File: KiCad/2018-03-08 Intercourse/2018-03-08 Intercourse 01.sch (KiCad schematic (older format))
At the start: 15 parts

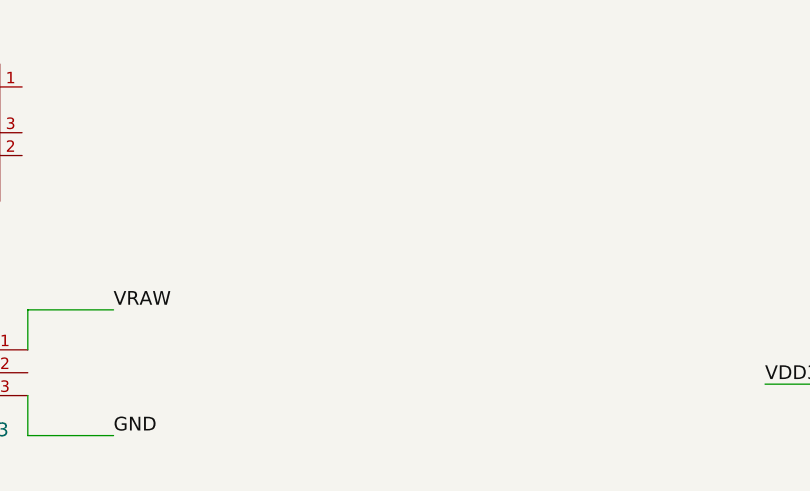
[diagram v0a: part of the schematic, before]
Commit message: added supercap charger
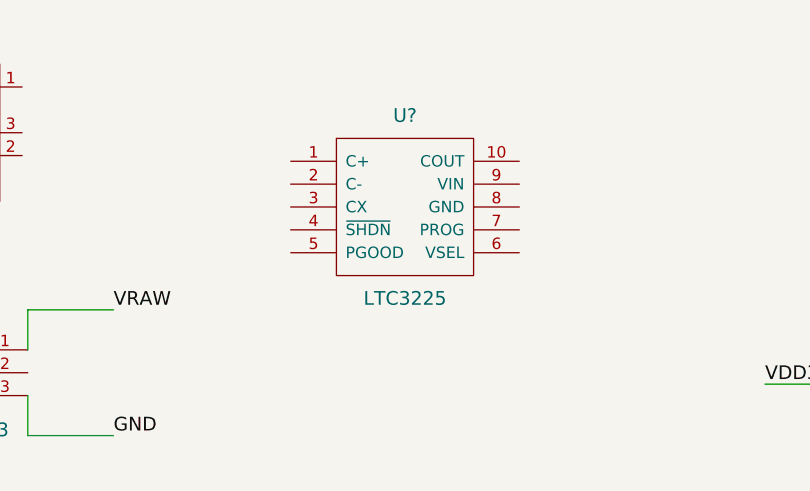
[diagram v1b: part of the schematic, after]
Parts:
- added U?: LTC3225, symbol LTC3225
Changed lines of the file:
@@
 LIBS:w25q-flash
 LIBS:murata-dmf3-supercap
+LIBS:LTC3225
 LIBS:2018-03-08 Intercourse 01-cache
 EELAYER 25 0
@@
 Wire Wire Line
 	1800 2425 1800 2300
+$Comp
+L LTC3225 U?
+U 1 1 5AAA787C
+P 3775 2225
+F 0 "U?" H 3775 2625 60  0000 C CNN
+F 1 "LTC3225" H 3775 1825 60  0000 C CNN
+F 2 "" H 3775 2225 60  0001 C CNN
+F 3 "" H 3775 2225 60  0001 C CNN
+	1    3775 2225
+	1    0    0    -1
+$EndComp
 $EndSCHEMATC

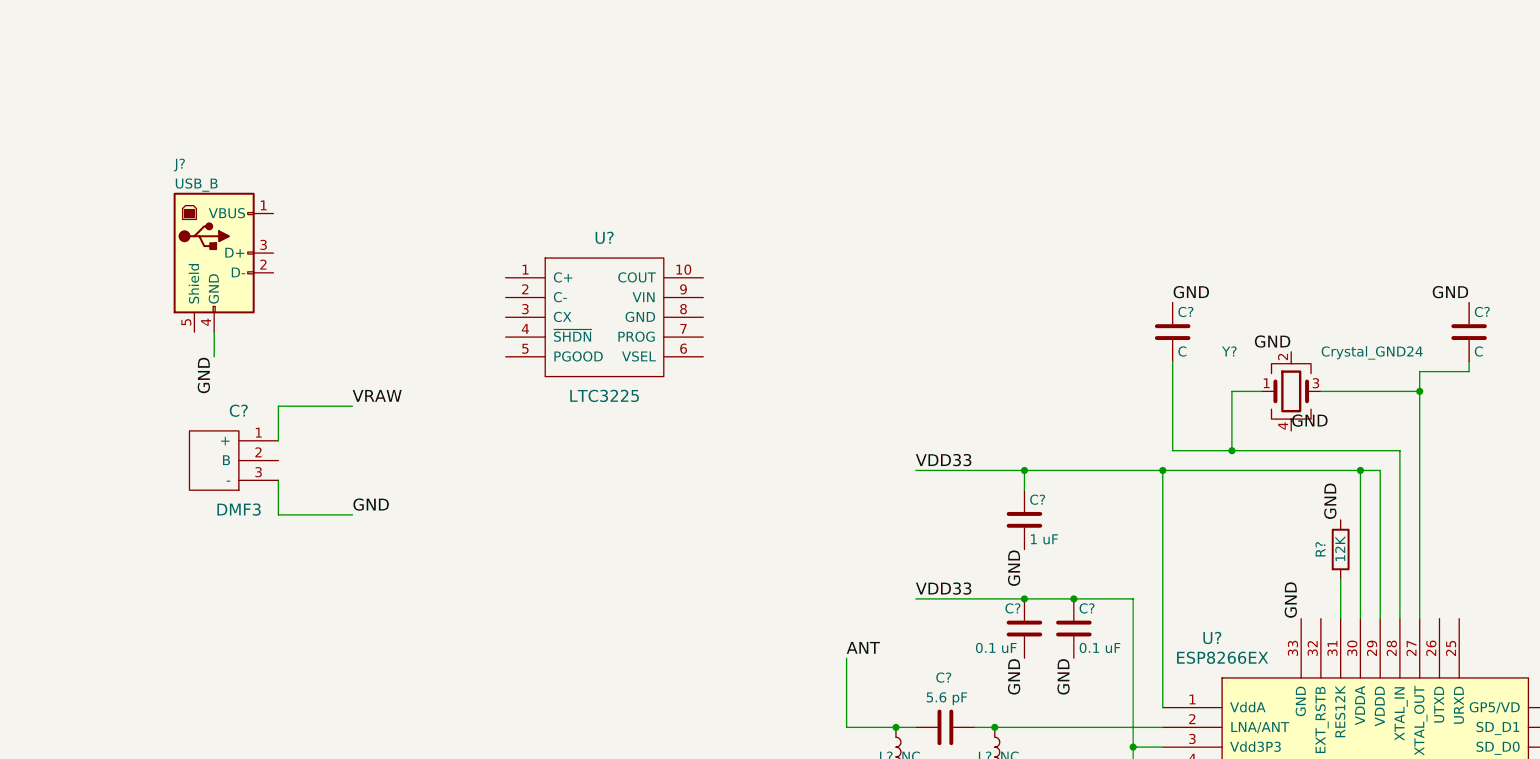
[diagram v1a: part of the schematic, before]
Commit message: added charge pump into schematic
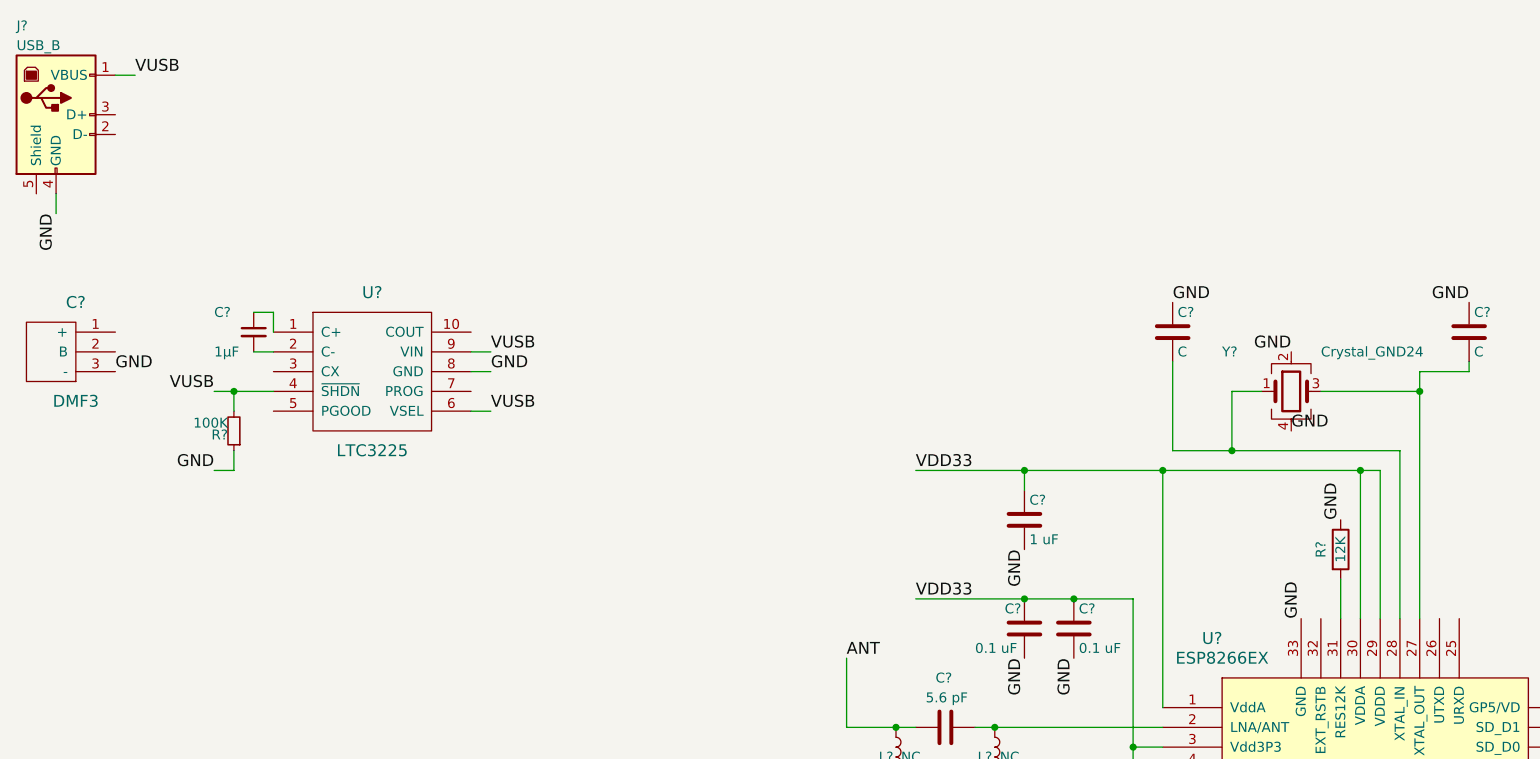
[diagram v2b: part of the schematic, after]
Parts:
- removed C?: DMF3, symbol DMF3
- removed J?: USB_B, symbol USB_B
- removed U?: LTC3225, symbol LTC3225
- added C?: DMF3, symbol DMF3
- added C?: 1μF, symbol C_Small
- added J?: USB_B, symbol USB_B
- added R?: 100K, symbol R_Small
- added U?: LTC3225, symbol LTC3225
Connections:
- net GND: now also C?.3 (-), J?.4 (GND), R?.1, U?.8 (GND)
- new net: C?.1, U?.1 (C+)
- new net: C?.2, U?.2 (C-)
- new net VUSB: J?.1 (VBUS), R?.2, U?.4 (~SHDN), U?.6 (VSEL), U?.9 (VIN)
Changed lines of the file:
@@
 	7800 2900 7800 3750
 Wire Wire Line
-	7800 2900 6650 2900
+	6650 2900 7800 2900
 Wire Wire Line
 	6650 2900 6650 2450
@@
 $EndComp
 Wire Wire Line
-	7700 3750 7700 3000
-Wire Wire Line
-	7700 3000 5350 3000
+	7700 3000 7700 3750
+Wire Wire Line
+	5350 3000 7700 3000
 Wire Wire Line
 	5900 3100 5900 3000
@@
 $Comp
 L DMF3 C?
-U 1 1 5AA8219C
-P 1925 2950
-F 0 "C?" H 1925 3200 60  0000 C CNN
-F 1 "DMF3" H 1925 2700 60  0000 C CNN
-F 2 "" H 1925 2950 60  0001 C CNN
-F 3 "" H 1925 2950 60  0001 C CNN
-	1    1925 2950
-	1    0    0    -1
-$EndComp
-Text Label 2500 3225 0    60   ~ 0
-GND
-Text Label 2500 2675 0    60   ~ 0
-VRAW
-Wire Wire Line
-	2125 2850 2125 2675
-Wire Wire Line
-	2125 2675 2500 2675
-Wire Wire Line
-	2500 3225 2125 3225
-Wire Wire Line
-	2125 3225 2125 3050
+U 1 1 5AAA8D1F
+P 1100 2400
+F 0 "C?" H 1100 2650 60  0000 C CNN
+F 1 "DMF3" H 1100 2150 60  0000 C CNN
+F 2 "" H 1100 2400 60  0001 C CNN
+F 3 "" H 1100 2400 60  0001 C CNN
+	1    1100 2400
+	1    0    0    -1
+$EndComp
+$Comp
+L LTC3225 U?
+U 1 1 5AAA8D7A
+P 2600 2500
+F 0 "U?" H 2600 2900 60  0000 C CNN
+F 1 "LTC3225" H 2600 2100 60  0000 C CNN
+F 2 "" H 2600 2500 60  0001 C CNN
+F 3 "" H 2600 2500 60  0001 C CNN
+	1    2600 2500
+	1    0    0    -1
+$EndComp
 $Comp
 L USB_B J?
-U 1 1 5AA82809
-P 1800 1900
-F 0 "J?" H 1600 2350 50  0000 L CNN
-F 1 "USB_B" H 1600 2250 50  0000 L CNN
-F 2 "" H 1950 1850 50  0001 C CNN
-F 3 "" H 1950 1850 50  0001 C CNN
-	1    1800 1900
-	1    0    0    -1
-$EndComp
-Text Label 1800 2425 3    60   ~ 0
-GND
-Wire Wire Line
-	1800 2425 1800 2300
-$Comp
-L LTC3225 U?
-U 1 1 5AAA787C
-P 3775 2225
-F 0 "U?" H 3775 2625 60  0000 C CNN
-F 1 "LTC3225" H 3775 1825 60  0000 C CNN
-F 2 "" H 3775 2225 60  0001 C CNN
-F 3 "" H 3775 2225 60  0001 C CNN
-	1    3775 2225
-	1    0    0    -1
-$EndComp
+U 1 1 5AAA8DD1
+P 1000 1200
+F 0 "J?" H 800 1650 50  0000 L CNN
+F 1 "USB_B" H 800 1550 50  0000 L CNN
+F 2 "" H 1150 1150 50  0001 C CNN
+F 3 "" H 1150 1150 50  0001 C CNN
+	1    1000 1200
+	1    0    0    -1
+$EndComp
+Text Label 1000 1700 3    60   ~ 0
+GND
+Text Label 3200 2700 0    60   ~ 0
+VUSB
+Wire Wire Line
+	1000 1600 1000 1700
+Wire Wire Line
+	1300 1000 1400 1000
+Text Label 1300 2500 0    60   ~ 0
+GND
+Text Label 3200 2500 0    60   ~ 0
+GND
+Wire Wire Line
+	3100 2500 3200 2500
+Wire Wire Line
+	3100 2700 3200 2700
+Text Label 1400 1000 0    60   ~ 0
+VUSB
+$Comp
+L C_Small C?
+U 1 1 5AAA95FB
+P 2000 2300
+F 0 "C?" H 1800 2400 50  0000 L CNN
+F 1 "1μF" H 1800 2200 50  0000 L CNN
+F 2 "" H 2000 2300 50  0001 C CNN
+F 3 "" H 2000 2300 50  0001 C CNN
+	1    2000 2300
+	1    0    0    -1
+$EndComp
+Wire Wire Line
+	2000 2200 2100 2200
+Wire Wire Line
+	2100 2200 2100 2300
+Wire Wire Line
+	2100 2400 2000 2400
+Text Label 3200 2400 0    60   ~ 0
+VUSB
+Wire Wire Line
+	3200 2400 3100 2400
+Text Label 1800 2600 2    60   ~ 0
+VUSB
+Wire Wire Line
+	1800 2600 2100 2600
+Wire Wire Line
+	1900 2600 1900 2700
+Connection ~ 1900 2600
+$Comp
+L R_Small R?
+U 1 1 5AAAA249
+P 1900 2800
+F 0 "R?" H 1930 2820 50  0000 L CNN
+F 1 "100K" H 1930 2760 50  0000 L CNN
+F 2 "" H 1900 2800 50  0001 C CNN
+F 3 "" H 1900 2800 50  0001 C CNN
+	1    1900 2800
+	-1   0    0    1
+$EndComp
+Wire Wire Line
+	1900 2900 1900 3000
+Wire Wire Line
+	1900 3000 1800 3000
+Text Label 1800 3000 2    60   ~ 0
+GND
 $EndSCHEMATC

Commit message: charge pump done
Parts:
- added C?: 2.2μF, symbol C_Small
- added D?: LED, symbol LED
- added Q?: P Channel, TO_SOT_Packages_SMD:SOT-23, symbol TP0610T
- added R?: 12K, symbol R_Small
- added R? (x2): 100K, symbol R_Small
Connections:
- net GND: now also C?.2, D?.1 (K), R?.2
- net VUSB: now also C?.1, Q?.2 (S), R?.1
- net at C?.1 (+): now also U?.10 (COUT)
- net at C?.2 (B): now also U?.3 (CX)
- net at U?.5 (PGOOD): now also Q?.1 (G), R?.2
- net at U?.7 (PROG): now also R?.1
- new net: Q?.3 (D), R?.1
- new net: D?.2 (A), R?.2
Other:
- note added: "Decoupling for LTC3225"
- note added: "Fully charged indicator"
- moved on the sheet: C?, R?, U?

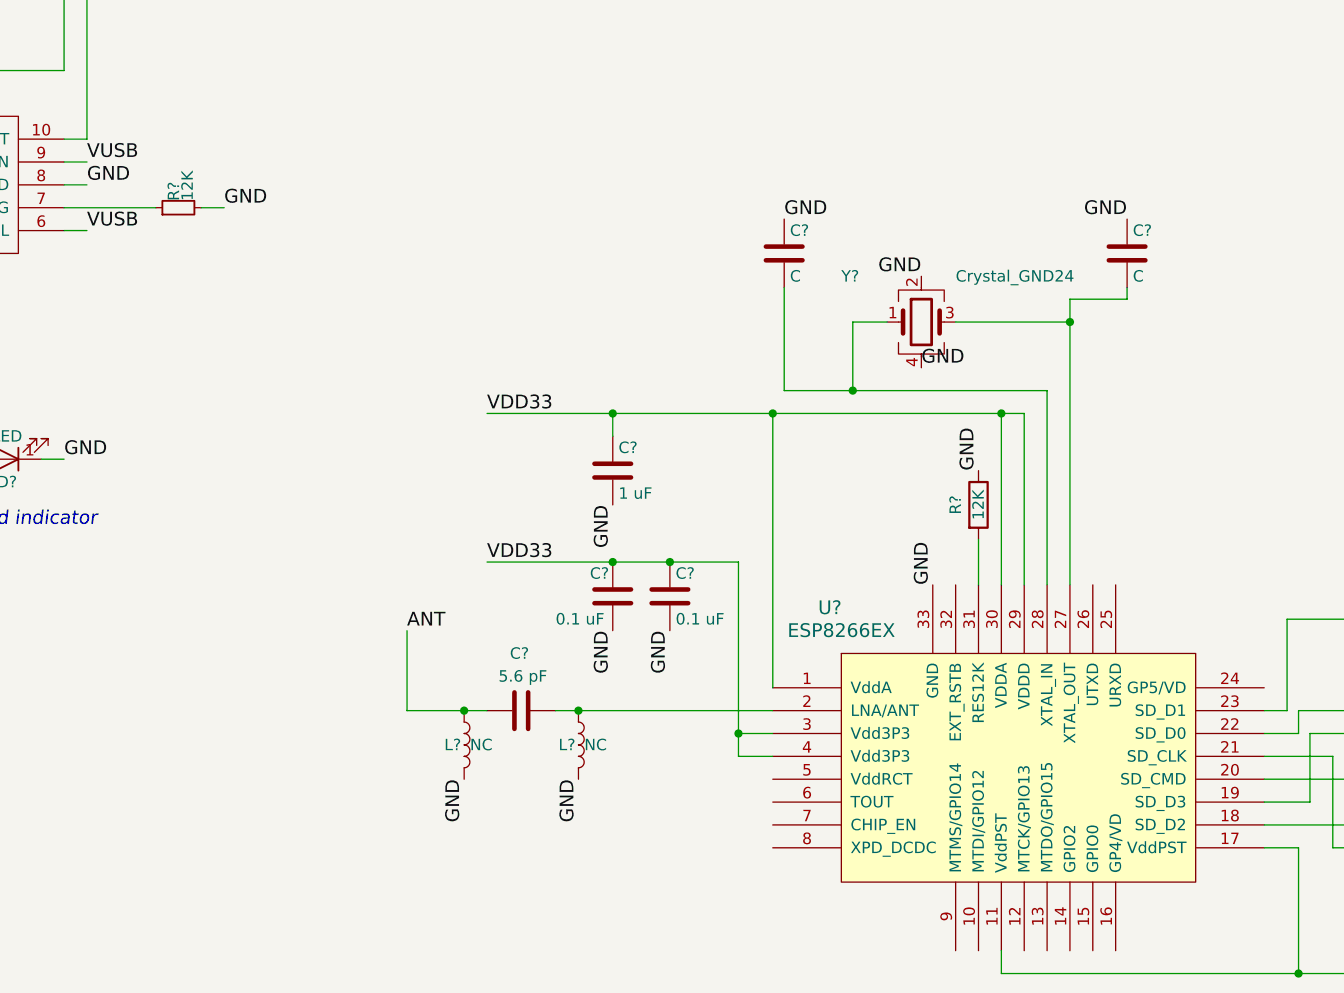
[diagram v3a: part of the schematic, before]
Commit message: Update Schematic
* Add missing Cap Values
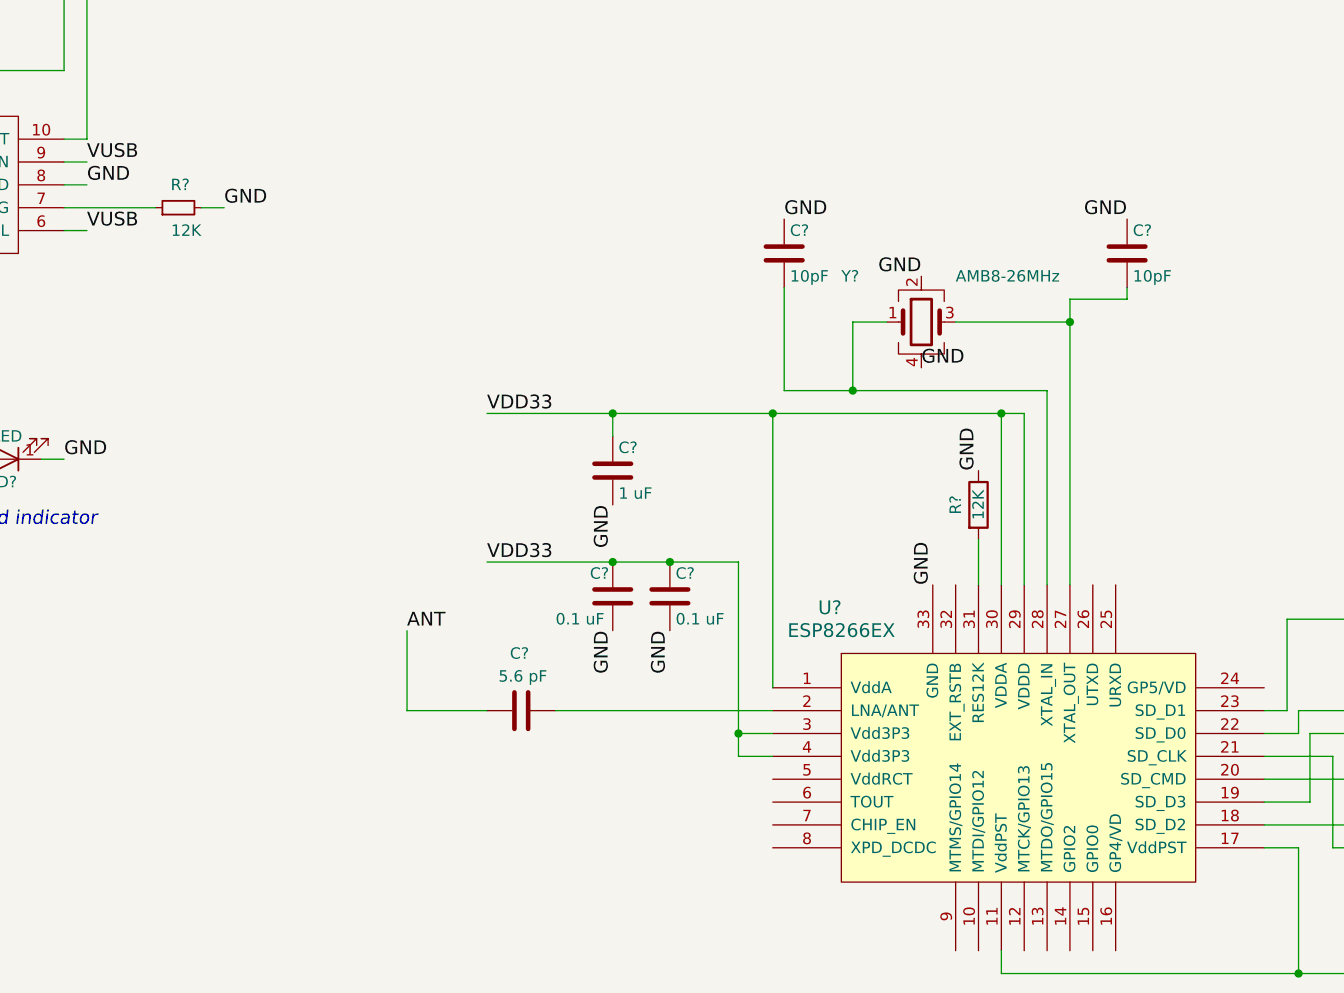
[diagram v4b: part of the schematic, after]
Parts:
- removed L? (x2): NC, symbol L
- C? (x2): value C -> 10pF
- Y?: value Crystal_GND24 -> AMB8-26MHz
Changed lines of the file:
@@
 P 7250 2600
 F 0 "Y?" H 6900 2800 50  0000 L CNN
-F 1 "Crystal_GND24" H 7400 2800 50  0000 L CNN
+F 1 "AMB8-26MHz" H 7400 2800 50  0000 L CNN
 F 2 "" H 7250 2600 50  0001 C CNN
 F 3 "" H 7250 2600 50  0001 C CNN
@@
 P 8150 2300
 F 0 "C?" H 8175 2400 50  0000 L CNN
-F 1 "C" H 8175 2200 50  0000 L CNN
+F 1 "10pF" H 8175 2200 50  0000 L CNN
 F 2 "" H 8188 2150 50  0001 C CNN
 F 3 "" H 8150 2300 50  0001 C CNN
@@
 P 6650 2300
 F 0 "C?" H 6675 2400 50  0000 L CNN
-F 1 "C" H 6675 2200 50  0000 L CNN
+F 1 "10pF" H 6675 2200 50  0000 L CNN
 F 2 "" H 6688 2150 50  0001 C CNN
 F 3 "" H 6650 2300 50  0001 C CNN
@@
 Text Label 7300 3750 1    60   ~ 0
 GND
-$Comp
-L L L?
-U 1 1 5AA80CE7
-P 5250 4450
-F 0 "L?" H 5200 4450 50  0000 C CNN
-F 1 "NC" H 5325 4450 50  0000 C CNN
-F 2 "" H 5250 4450 50  0001 C CNN
-F 3 "" H 5250 4450 50  0001 C CNN
-	1    5250 4450
-	1    0    0    -1
-$EndComp
-$Comp
-L L L?
-U 1 1 5AA80D86
-P 5750 4450
-F 0 "L?" H 5700 4450 50  0000 C CNN
-F 1 "NC" H 5825 4450 50  0000 C CNN
-F 2 "" H 5750 4450 50  0001 C CNN
-F 3 "" H 5750 4450 50  0001 C CNN
-	1    5750 4450
-	1    0    0    -1
-$EndComp
 $Comp
 L C C?
@@
 Text Label 5000 3950 0    60   ~ 0
 ANT
-Text Label 5250 4600 3    60   ~ 0
-GND
-Text Label 5750 4600 3    60   ~ 0
-GND
 $Comp
 L C C?
@@
 U 1 1 5AAAACAB
 P 4000 2100
-F 0 "R?" H 4030 2120 50  0000 L CNN
-F 1 "12K" H 4030 2060 50  0000 L CNN
+F 0 "R?" V 4100 2050 50  0000 L CNN
+F 1 "12K" V 3900 2000 50  0000 L CNN
 F 2 "" H 4000 2100 50  0001 C CNN
 F 3 "" H 4000 2100 50  0001 C CNN
@@
 Wire Wire Line
 	5650 4300 6600 4300
-Connection ~ 5750 4300
 Wire Wire Line
 	5000 4300 5350 4300
 Wire Wire Line
 	5000 3950 5000 4300
-Connection ~ 5250 4300
 Wire Wire Line
 	5350 3650 6450 3650
